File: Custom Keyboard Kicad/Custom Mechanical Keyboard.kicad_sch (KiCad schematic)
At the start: 288 parts, among them J1 USB_C_Receptacle_USB2.0_16P, J2 Conn_01x04, J3 Conn_01x05, J4 Conn_01x06, J5 Conn_01x07, J6 Conn_01x20_Socket, J7 Conn_01x20_Socket, SW1 SW_SPST, SW10 SW_SPST, SW11 SW_SPST, SW12 SW_SPST, SW13 SW_SPST, SW14 SW_SPST, SW15 SW_SPST, SW16 SW_SPST, SW17 SW_SPST, SW18 SW_SPST, SW19 SW_SPST, SW2 SW_SPST, SW20 SW_SPST, SW21 SW_SPST, SW22 SW_SPST, SW23 SW_SPST, SW24 SW_SPST, SW25 SW_SPST, SW26 SW_SPST, SW27 SW_SPST, SW28 SW_SPST, SW29 SW_SPST, SW3 SW_SPST, SW30 SW_SPST, SW31 SW_SPST, SW32 SW_SPST, SW33 SW_SPST, SW34 SW_SPST, SW35 SW_SPST, SW36 SW_SPST, SW37 SW_SPST, SW38 SW_SPST, SW39 SW_SPST, SW4 SW_SPST, SW40 SW_SPST, SW41 SW_SPST, SW42 SW_SPST, SW43 SW_SPST, SW44 SW_SPST, SW45 SW_SPST, SW46 SW_SPST, SW47 SW_SPST, SW48 SW_SPST, SW49 SW_SPST, SW5 SW_SPST, SW50 SW_SPST, SW51 SW_SPST, SW52 SW_SPST, SW53 SW_SPST, SW54 SW_SPST, SW55 SW_SPST, SW56 SW_SPST, SW57 SW_SPST, SW58 SW_SPST, SW59 SW_SPST, SW6 SW_SPST, SW60 SW_SPST, SW61 SW_SPST, SW62 SW_SPST, SW63 SW_SPST, SW64 SW_SPST, SW65 SW_SPST, SW66 SW_SPST, SW67 SW_SPST, SW68 SW_SPST, SW69 SW_SPST, SW7 SW_SPST, SW70 SW_SPST, SW71 SW_SPST, SW72 SW_SPST, SW73 SW_SPST, SW74 SW_SPST, SW75 SW_SPST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

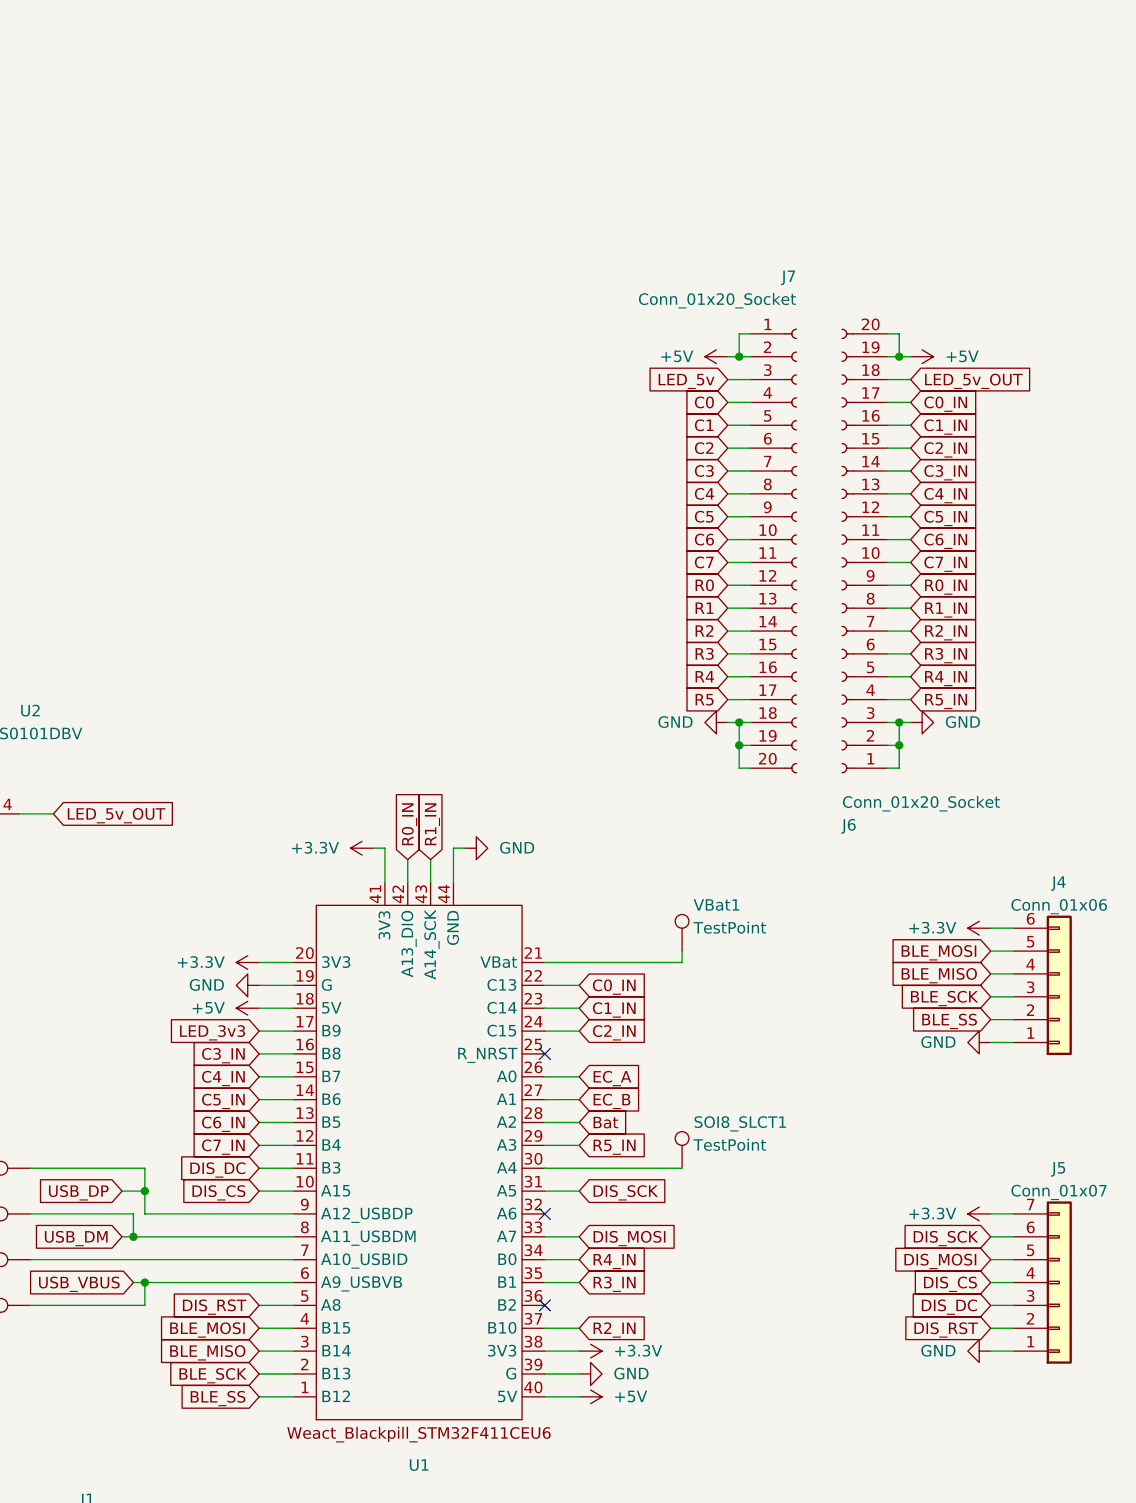
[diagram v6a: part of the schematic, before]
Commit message: Fixed DRC issues, shifted MCU side FPC connector to face opposite way (ribbon cable goes around and under MCU pcb).
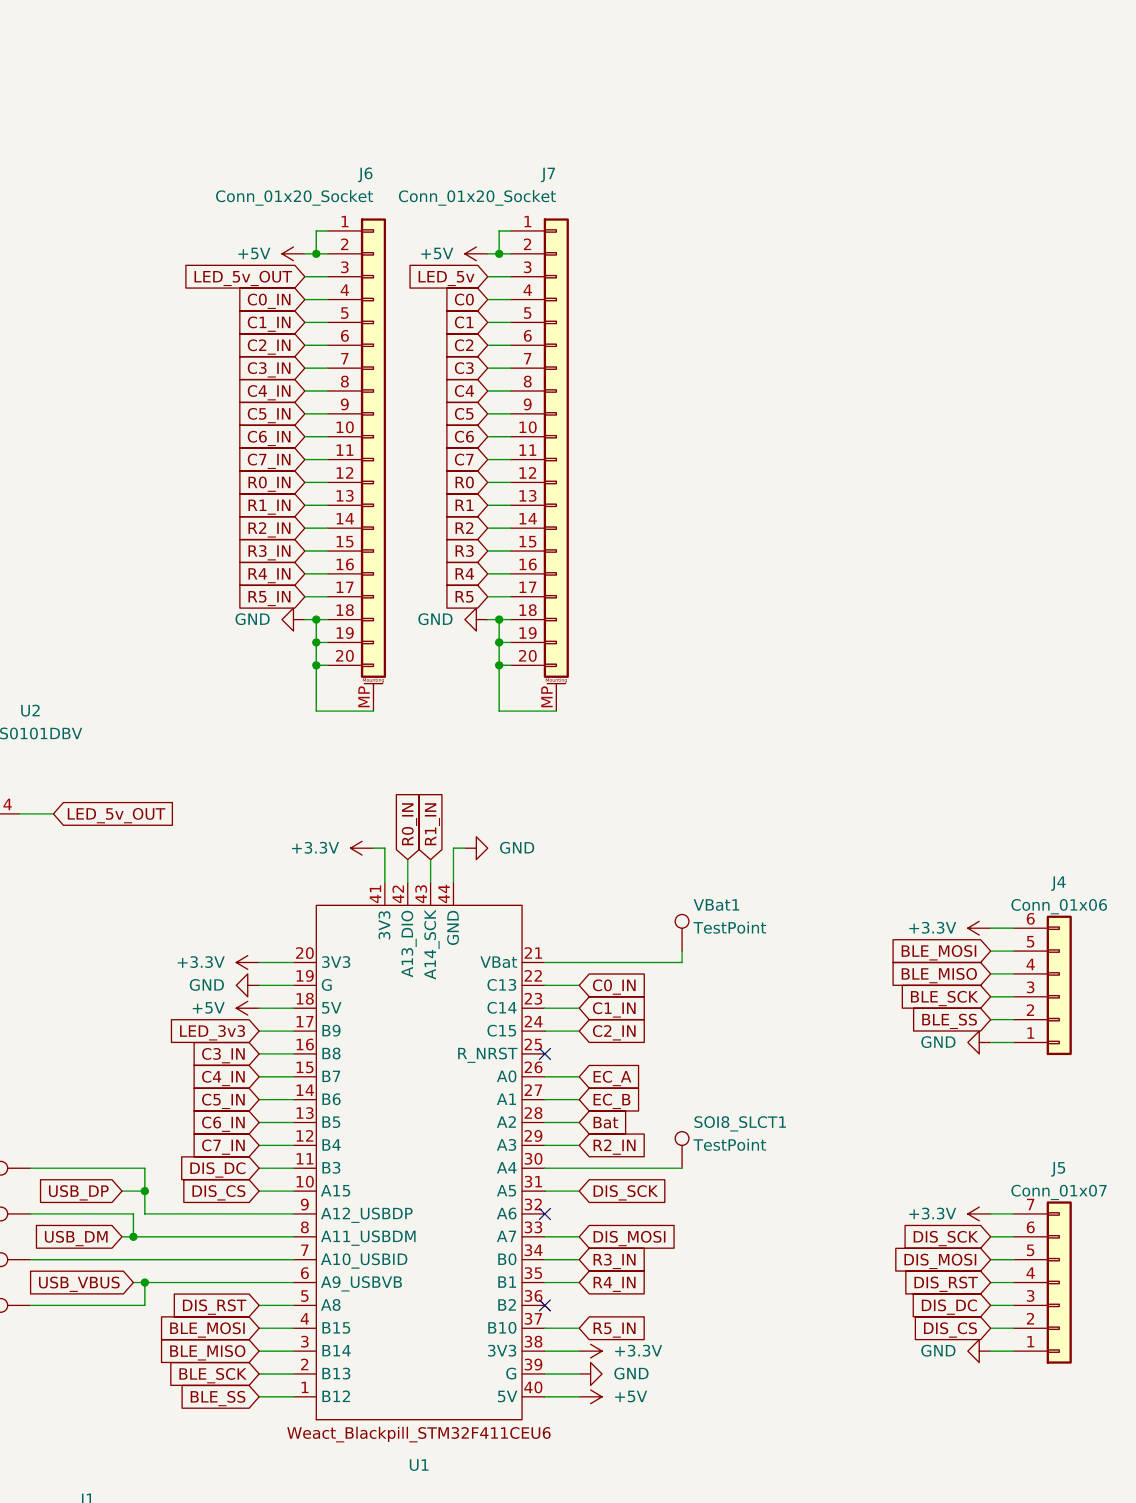
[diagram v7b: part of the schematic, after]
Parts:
- J6, J7: symbol Connector:Conn_01x20_Socket -> Connector_Generic_MountingPin:Conn_01x20_MountingPin
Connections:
- net +5V: now also J6.1 (Pin_1), J6.2 (Pin_2); no longer J6.19 (Pin_19), J6.20 (Pin_20)
- net C0_IN: now also J6.4 (Pin_4); no longer J6.17 (Pin_17)
- net C1_IN: now also J6.5 (Pin_5); no longer J6.16 (Pin_16)
- net C2_IN: now also J6.6 (Pin_6); no longer J6.15 (Pin_15)
- net C3_IN: now also J6.7 (Pin_7); no longer J6.14 (Pin_14)
- net C4_IN: now also J6.8 (Pin_8); no longer J6.13 (Pin_13)
- net C5_IN: now also J6.9 (Pin_9); no longer J6.12 (Pin_12)
- net C6_IN: now also J6.10 (Pin_10); no longer J6.11 (Pin_11)
- net C7_IN: now also J6.11 (Pin_11); no longer J6.10 (Pin_10)
- net DIS_CS: now also J5.2 (Pin_2); no longer J5.4 (Pin_4)
- net DIS_RST: now also J5.4 (Pin_4); no longer J5.2 (Pin_2)
- net GND: now also J6.18 (Pin_18), J6.19 (Pin_19), J6.20 (Pin_20), J6.MP (MountPin), J7.MP (MountPin); no longer J6.1 (Pin_1), J6.2 (Pin_2), J6.3 (Pin_3)
- net LED_5v_OUT: now also J6.3 (Pin_3); no longer J6.18 (Pin_18)
- net R0_IN: now also J6.12 (Pin_12); no longer J6.9 (Pin_9)
- net R1_IN: now also J6.13 (Pin_13); no longer J6.8 (Pin_8)
- net R2_IN: now also J6.14 (Pin_14), U1.29 (A3); no longer J6.7 (Pin_7), U1.37 (B10)
- net R3_IN: now also J6.15 (Pin_15), U1.34 (B0); no longer J6.6 (Pin_6), U1.35 (B1)
- net R4_IN: now also J6.16 (Pin_16), U1.35 (B1); no longer J6.5 (Pin_5), U1.34 (B0)
- net R5_IN: now also J6.17 (Pin_17), U1.37 (B10); no longer J6.4 (Pin_4), U1.29 (A3)

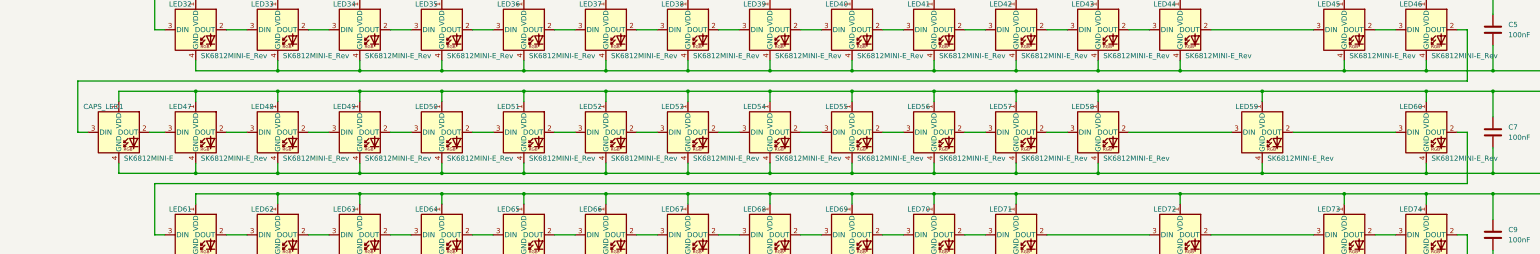
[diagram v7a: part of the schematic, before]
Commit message: feat: Swapped capslock LED to bottom (same as LED matrix)
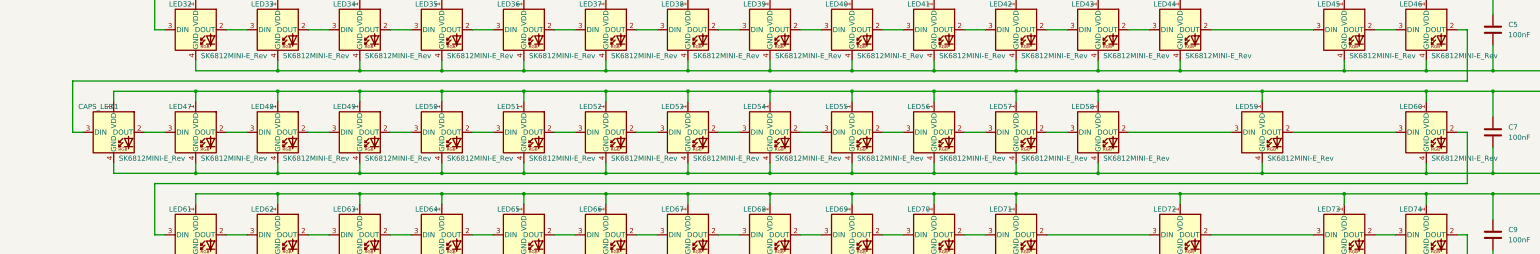
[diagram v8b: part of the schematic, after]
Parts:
- CAPS_LED1: value SK6812MINI-E -> SK6812MINI-E_Rev; footprint LED_SMD:LED_SK6812MINI-E_PLCC4_3.2x2.8mm_P1.5mm_1 -> LED_SMD:LED_SK6812MINI-E_Reversed_PLCC4_3.2x2.8mm_P1.5mm
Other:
- moved on the sheet: CAPS_LED1
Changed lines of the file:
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@@
 	(wire
 		(pts
-			(xy 50.8 264.16) (xy 50.8 261.62)
+			(xy 49.53 264.16) (xy 49.53 261.62)
 		)
 		(stroke
@@
 	(wire
 		(pts
-			(xy 40.64 259.08) (xy 384.81 259.08)
+			(xy 39.37 259.08) (xy 384.81 259.08)
 		)
 		(stroke
@@
 	(wire
 		(pts
-			(xy 40.64 271.78) (xy 40.64 259.08)
+			(xy 39.37 271.78) (xy 39.37 259.08)
 		)
 		(stroke
@@
 	(wire
 		(pts
-			(xy 50.8 279.4) (xy 50.8 281.94)
+			(xy 49.53 279.4) (xy 49.53 281.94)
 		)
 		(stroke
@@
 	(wire
 		(pts
-			(xy 50.8 261.62) (xy 69.85 261.62)
+			(xy 49.53 261.62) (xy 69.85 261.62)
 		)
 		(stroke
@@
 	(wire
 		(pts
-			(xy 58.42 271.78) (xy 62.23 271.78)
+			(xy 57.15 271.78) (xy 62.23 271.78)
 		)
 		(stroke
@@
 	(wire
 		(pts
-			(xy 50.8 281.94) (xy 69.85 281.94)
+			(xy 49.53 281.94) (xy 69.85 281.94)
 		)
 		(stroke
@@
 	(wire
 		(pts
-			(xy 40.64 271.78) (xy 43.18 271.78)
+			(xy 39.37 271.78) (xy 41.91 271.78)
 		)
 		(stroke
@@
 	(symbol
 		(lib_id "LED_SMD:SK6812MINI-E")
-		(at 50.8 271.78 0)
+		(at 49.53 271.78 0)
 		(unit 1)
 		(exclude_from_sim no)
@@
 		(dnp no)
 		(property "Reference" "CAPS_LED1"
-			(at 46.99 265.43 0)
+			(at 45.72 265.43 0)
 			(effects
 				(font
@@
 			)
 		)
-		(property "Value" "SK6812MINI-E"
-			(at 52.07 277.495 0)
+		(property "Value" "SK6812MINI-E_Rev"
+			(at 50.8 277.495 0)
 			(effects
 				(font
@@
 			)
 		)
-		(property "Footprint" "LED_SMD:LED_SK6812MINI-E_PLCC4_3.2x2.8mm_P1.5mm_1"
-			(at 52.07 279.4 0)
+		(property "Footprint" "LED_SMD:LED_SK6812MINI-E_Reversed_PLCC4_3.2x2.8mm_P1.5mm"
+			(at 50.8 279.4 0)
 			(effects
 				(font
@@
 		)
 		(property "Datasheet" "https://cdn-shop.adafruit.com/product-files/4960/4960_SK6812MINI-E_REV02_EN.pdf"
-			(at 53.34 281.305 0)
+			(at 52.07 281.305 0)
 			(effects
 				(font
@@
 		)
 		(property "Description" "3.2x2.8x1.78 mm 0.2W Intelligent external control surface  mount SMD LED (Facing away from PCB)"
-			(at 50.8 271.78 0)
+			(at 49.53 271.78 0)
 			(effects
 				(font
@@
 		)
 		(property "MFG Part #" " SK6803MINI-E"
-			(at 50.8 271.78 0)
+			(at 49.53 271.78 0)
 			(effects
 				(font
@@
 		)
 		(property "Manufacturer" "Shenzhen Normand Electronic"
-			(at 50.8 271.78 0)
+			(at 49.53 271.78 0)
 			(effects
 				(font
@@
 		)
 		(property "Type" "SMD"
-			(at 50.8 271.78 0)
+			(at 49.53 271.78 0)
 			(effects
 				(font
